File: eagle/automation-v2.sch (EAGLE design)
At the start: 103 parts, among them IC1 MEGA48/88/168-AU, IC2 DS2482-100S, IC3 DS2482-100S, IC4 78L33, K1 SRD-05VDC-SL-C, K2 SRD-05VDC-SL-C, K3 SRD-05VDC-SL-C, K4 SRD-05VDC-SL-C, Q1 BSS123, Q2 BSS123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

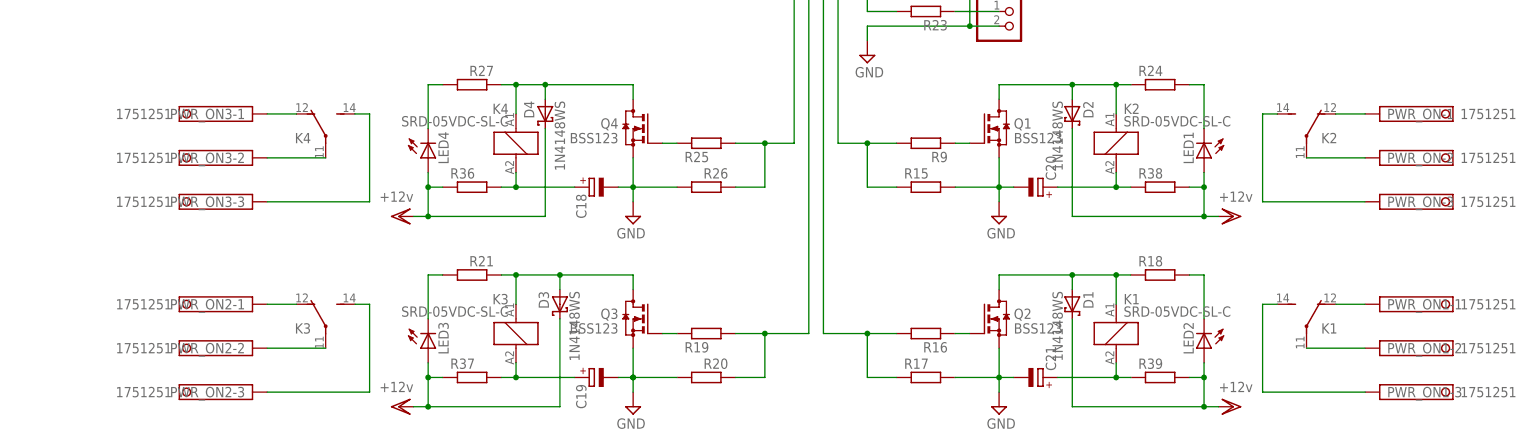
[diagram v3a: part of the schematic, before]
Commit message: Replace screw clamps
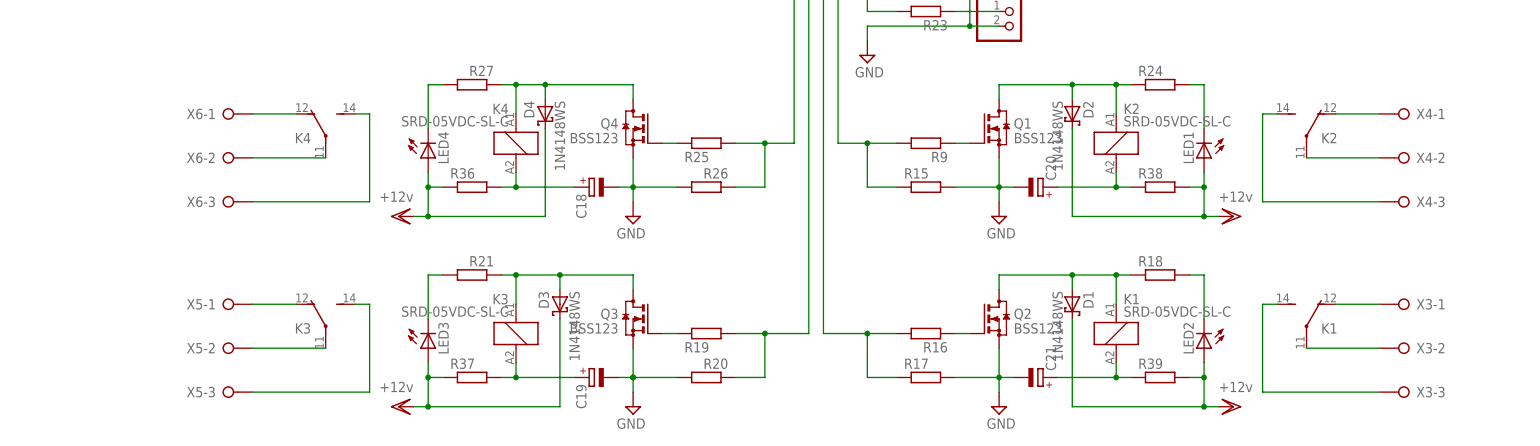
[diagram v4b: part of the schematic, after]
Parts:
- removed PWR_ON, PWR_ON1, PWR_ON2, PWR_ON3: 1751251, con-phoenix-350:1751251
- added X3, X4, X5, X6: (no value), con-wago-508:W237-03P
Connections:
- net N$28: now also X4-2.KL; no longer PWR_ON-2.K
- net N$32: now also X4-3.KL; no longer PWR_ON-3.K
- net N$33: now also X4-1.KL; no longer PWR_ON-1.K
- net N$42: now also X3-2.KL; no longer PWR_ON1-2.K
- net N$44: now also X3-3.KL; no longer PWR_ON1-3.K
- net N$45: now also X3-1.KL; no longer PWR_ON1-1.K
- net N$50: now also X5-2.KL; no longer PWR_ON2-2.K
- net N$51: now also X5-3.KL; no longer PWR_ON2-3.K
- net N$52: now also X5-1.KL; no longer PWR_ON2-1.K
- net N$57: now also X6-2.KL; no longer PWR_ON3-2.K
- net N$58: now also X6-3.KL; no longer PWR_ON3-3.K
- net N$59: now also X6-1.KL; no longer PWR_ON3-1.K
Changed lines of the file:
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@@
 <part name="R24" library="rcl" deviceset="R-EU_" device="R0603"/>
 <part name="LED1" library="led" deviceset="LED" device="SML0805"/>
-<part name="PWR_ON" library="con-phoenix-350" deviceset="1751251" device=""/>
 <part name="V12" library="supply1" deviceset="VDD" device="" value="+12v"/>
 <part name="V1" library="supply1" deviceset="VDD" device="" value="+12v"/>
@@
 <part name="R18" library="rcl" deviceset="R-EU_" device="R0603"/>
 <part name="LED2" library="led" deviceset="LED" device="SML0805"/>
-<part name="PWR_ON1" library="con-phoenix-350" deviceset="1751251" device=""/>
 <part name="V2" library="supply1" deviceset="VDD" device="" value="+12v"/>
 <part name="Q3" library="transistor-small-signal" deviceset="BSS123" device=""/>
@@
 <part name="R21" library="rcl" deviceset="R-EU_" device="R0603"/>
 <part name="LED3" library="led" deviceset="LED" device="SML0805"/>
-<part name="PWR_ON2" library="con-phoenix-350" deviceset="1751251" device=""/>
 <part name="V3" library="supply1" deviceset="VDD" device="" value="+12v"/>
 <part name="Q4" library="transistor-small-signal" deviceset="BSS123" device=""/>
@@
 <part name="R27" library="rcl" deviceset="R-EU_" device="R0603"/>
 <part name="LED4" library="led" deviceset="LED" device="SML0805"/>
-<part name="PWR_ON3" library="con-phoenix-350" deviceset="1751251" device=""/>
 <part name="V4" library="supply1" deviceset="VDD" device="" value="+12v"/>
 <part name="D5" library="diode" deviceset="CGRM400*-G" device="" technology="1"/>
@@
 <part name="C21" library="rcl" deviceset="CPOL-EU" device="E5-10.5"/>
 <part name="C22" library="rcl" deviceset="C-EU" device="C0805" value="0.1"/>
+<part name="X3" library="con-wago-508" deviceset="W237-03P" device=""/>
+<part name="X4" library="con-wago-508" deviceset="W237-03P" device=""/>
+<part name="X5" library="con-wago-508" deviceset="W237-03P" device=""/>
+<part name="X6" library="con-wago-508" deviceset="W237-03P" device=""/>
 </parts>
 <sheets>
@@
 <instance part="R24" gate="G$1" x="22.86" y="-35.56"/>
 <instance part="LED1" gate="G$1" x="30.48" y="-48.26" rot="R180"/>
-<instance part="PWR_ON" gate="-1" x="60.96" y="-40.64"/>
-<instance part="PWR_ON" gate="-2" x="60.96" y="-48.26"/>
-<instance part="PWR_ON" gate="-3" x="60.96" y="-55.88"/>
 <instance part="V12" gate="G$1" x="35.56" y="-58.42" rot="R270"/>
 <instance part="V1" gate="G$1" x="-185.42" y="121.92" rot="R90"/>
@@
 <instance part="R18" gate="G$1" x="22.86" y="-68.58"/>
 <instance part="LED2" gate="G$1" x="30.48" y="-81.28" rot="R180"/>
-<instance part="PWR_ON1" gate="-1" x="60.96" y="-73.66"/>
-<instance part="PWR_ON1" gate="-2" x="60.96" y="-81.28"/>
-<instance part="PWR_ON1" gate="-3" x="60.96" y="-88.9"/>
 <instance part="V2" gate="G$1" x="35.56" y="-91.44" rot="R270"/>
 <instance part="Q3" gate="G$1" x="-68.58" y="-76.2" rot="MR0"/>
@@
 <instance part="R21" gate="G$1" x="-96.52" y="-68.58" rot="MR0"/>
 <instance part="LED3" gate="G$1" x="-104.14" y="-81.28" rot="MR180"/>
-<instance part="PWR_ON2" gate="-1" x="-134.62" y="-73.66" rot="MR0"/>
-<instance part="PWR_ON2" gate="-2" x="-134.62" y="-81.28" rot="MR0"/>
-<instance part="PWR_ON2" gate="-3" x="-134.62" y="-88.9" rot="MR0"/>
 <instance part="V3" gate="G$1" x="-109.22" y="-91.44" rot="MR270"/>
 <instance part="Q4" gate="G$1" x="-68.58" y="-43.18" rot="MR0"/>
@@
 <instance part="R27" gate="G$1" x="-96.52" y="-35.56" rot="MR0"/>
 <instance part="LED4" gate="G$1" x="-104.14" y="-48.26" rot="MR180"/>
-<instance part="PWR_ON3" gate="-1" x="-134.62" y="-40.64" rot="MR0"/>
-<instance part="PWR_ON3" gate="-2" x="-134.62" y="-48.26" rot="MR0"/>
-<instance part="PWR_ON3" gate="-3" x="-134.62" y="-55.88" rot="MR0"/>
 <instance part="V4" gate="G$1" x="-109.22" y="-58.42" rot="MR270"/>
 <instance part="D5" gate="G$1" x="-187.96" y="45.72"/>
@@
 <instance part="C21" gate="G$1" x="2.54" y="-86.36" rot="MR90"/>
 <instance part="C22" gate="G$1" x="-71.12" y="104.14" rot="R180"/>
+<instance part="X3" gate="-1" x="66.04" y="-73.66" rot="R180"/>
+<instance part="X3" gate="-2" x="66.04" y="-81.28" rot="R180"/>
+<instance part="X3" gate="-3" x="66.04" y="-88.9" rot="R180"/>
+<instance part="X4" gate="-1" x="66.04" y="-40.64" rot="R180"/>
+<instance part="X4" gate="-2" x="66.04" y="-48.26" rot="R180"/>
+<instance part="X4" gate="-3" x="66.04" y="-55.88" rot="R180"/>
+<instance part="X5" gate="-1" x="-139.7" y="-73.66" rot="MR180"/>
+<instance part="X5" gate="-2" x="-139.7" y="-81.28" rot="MR180"/>
+<instance part="X5" gate="-3" x="-139.7" y="-88.9" rot="MR180"/>
+<instance part="X6" gate="-1" x="-139.7" y="-40.64" rot="MR180"/>
+<instance part="X6" gate="-2" x="-139.7" y="-48.26" rot="MR180"/>
+<instance part="X6" gate="-3" x="-139.7" y="-55.88" rot="MR180"/>
 </instances>
 <busses>
@@
 <net name="N$28" class="2">
 <segment>
-<pinref part="PWR_ON" gate="-2" pin="K"/>
-<wire x1="48.26" y1="-48.26" x2="58.42" y2="-48.26" width="0.1524" layer="91"/>
+<wire x1="48.26" y1="-48.26" x2="60.96" y2="-48.26" width="0.1524" layer="91"/>
 <pinref part="K2" gate="2" pin="P"/>
+<pinref part="X4" gate="-2" pin="KL"/>
 </segment>
 </net>
 <net name="N$32" class="2">
 <segment>
-<pinref part="PWR_ON" gate="-3" pin="K"/>
-<wire x1="40.64" y1="-55.88" x2="58.42" y2="-55.88" width="0.1524" layer="91"/>
+<wire x1="40.64" y1="-55.88" x2="60.96" y2="-55.88" width="0.1524" layer="91"/>
 <pinref part="K2" gate="2" pin="S"/>
 <wire x1="43.18" y1="-40.64" x2="40.64" y2="-40.64" width="0.1524" layer="91"/>
 <wire x1="40.64" y1="-40.64" x2="40.64" y2="-55.88" width="0.1524" layer="91"/>
+<pinref part="X4" gate="-3" pin="KL"/>
 </segment>
 </net>
 <net name="N$33" class="2">
 <segment>
-<pinref part="PWR_ON" gate="-1" pin="K"/>
-<wire x1="53.34" y1="-40.64" x2="58.42" y2="-40.64" width="0.1524" layer="91"/>
+<wire x1="53.34" y1="-40.64" x2="60.96" y2="-40.64" width="0.1524" layer="91"/>
 <pinref part="K2" gate="2" pin="O"/>
+<pinref part="X4" gate="-1" pin="KL"/>
 </segment>
 </net>
@@
 <net name="N$42" class="2">
 <segment>
-<pinref part="PWR_ON1" gate="-2" pin="K"/>
-<wire x1="48.26" y1="-81.28" x2="58.42" y2="-81.28" width="0.1524" layer="91"/>
+<wire x1="48.26" y1="-81.28" x2="60.96" y2="-81.28" width="0.1524" layer="91"/>
 <pinref part="K1" gate="2" pin="P"/>
+<pinref part="X3" gate="-2" pin="KL"/>
 </segment>
 </net>
 <net name="N$44" class="2">
 <segment>
-<pinref part="PWR_ON1" gate="-3" pin="K"/>
-<wire x1="40.64" y1="-88.9" x2="58.42" y2="-88.9" width="0.1524" layer="91"/>
+<wire x1="40.64" y1="-88.9" x2="60.96" y2="-88.9" width="0.1524" layer="91"/>
 <pinref part="K1" gate="2" pin="S"/>
 <wire x1="43.18" y1="-73.66" x2="40.64" y2="-73.66" width="0.1524" layer="91"/>
 <wire x1="40.64" y1="-73.66" x2="40.64" y2="-88.9" width="0.1524" layer="91"/>
+<pinref part="X3" gate="-3" pin="KL"/>
 </segment>
 </net>
 <net name="N$45" class="2">
 <segment>
-<pinref part="PWR_ON1" gate="-1" pin="K"/>
-<wire x1="53.34" y1="-73.66" x2="58.42" y2="-73.66" width="0.1524" layer="91"/>
+<wire x1="53.34" y1="-73.66" x2="60.96" y2="-73.66" width="0.1524" layer="91"/>
 <pinref part="K1" gate="2" pin="O"/>
+<pinref part="X3" gate="-1" pin="KL"/>
 </segment>
 </net>
@@
 <net name="N$50" class="2">
 <segment>
-<pinref part="PWR_ON2" gate="-2" pin="K"/>
-<wire x1="-121.92" y1="-81.28" x2="-132.08" y2="-81.28" width="0.1524" layer="91"/>
+<wire x1="-121.92" y1="-81.28" x2="-134.62" y2="-81.28" width="0.1524" layer="91"/>
 <pinref part="K3" gate="2" pin="P"/>
+<pinref part="X5" gate="-2" pin="KL"/>
 </segment>
 </net>
 <net name="N$51" class="2">
 <segment>
-<pinref part="PWR_ON2" gate="-3" pin="K"/>
-<wire x1="-114.3" y1="-88.9" x2="-132.08" y2="-88.9" width="0.1524" layer="91"/>
+<wire x1="-114.3" y1="-88.9" x2="-134.62" y2="-88.9" width="0.1524" layer="91"/>
 <pinref part="K3" gate="2" pin="S"/>
 <wire x1="-116.84" y1="-73.66" x2="-114.3" y2="-73.66" width="0.1524" layer="91"/>
 <wire x1="-114.3" y1="-73.66" x2="-114.3" y2="-88.9" width="0.1524" layer="91"/>
+<pinref part="X5" gate="-3" pin="KL"/>
 </segment>
 </net>
 <net name="N$52" class="2">
 <segment>
-<pinref part="PWR_ON2" gate="-1" pin="K"/>
-<wire x1="-127" y1="-73.66" x2="-132.08" y2="-73.66" width="0.1524" layer="91"/>
+<wire x1="-127" y1="-73.66" x2="-134.62" y2="-73.66" width="0.1524" layer="91"/>
 <pinref part="K3" gate="2" pin="O"/>
+<pinref part="X5" gate="-1" pin="KL"/>
 </segment>
 </net>
@@
 <net name="N$57" class="2">
 <segment>
-<pinref part="PWR_ON3" gate="-2" pin="K"/>
-<wire x1="-121.92" y1="-48.26" x2="-132.08" y2="-48.26" width="0.1524" layer="91"/>
+<wire x1="-121.92" y1="-48.26" x2="-134.62" y2="-48.26" width="0.1524" layer="91"/>
 <pinref part="K4" gate="2" pin="P"/>
+<pinref part="X6" gate="-2" pin="KL"/>
 </segment>
 </net>
 <net name="N$58" class="2">
 <segment>
-<pinref part="PWR_ON3" gate="-3" pin="K"/>
-<wire x1="-114.3" y1="-55.88" x2="-132.08" y2="-55.88" width="0.1524" layer="91"/>
+<wire x1="-114.3" y1="-55.88" x2="-134.62" y2="-55.88" width="0.1524" layer="91"/>
 <pinref part="K4" gate="2" pin="S"/>
 <wire x1="-116.84" y1="-40.64" x2="-114.3" y2="-40.64" width="0.1524" layer="91"/>
 <wire x1="-114.3" y1="-40.64" x2="-114.3" y2="-55.88" width="0.1524" layer="91"/>
+<pinref part="X6" gate="-3" pin="KL"/>
 </segment>
 </net>
 <net name="N$59" class="2">
 <segment>
-<pinref part="PWR_ON3" gate="-1" pin="K"/>
-<wire x1="-127" y1="-40.64" x2="-132.08" y2="-40.64" width="0.1524" layer="91"/>
+<wire x1="-127" y1="-40.64" x2="-134.62" y2="-40.64" width="0.1524" layer="91"/>
 <pinref part="K4" gate="2" pin="O"/>
-</segment>
-</net>
+<pinref part="X6" gate="-1" pin="KL"/>
+</segment>
+</net>
